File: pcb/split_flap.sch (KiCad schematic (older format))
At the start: 53 parts, among them T1 MPSA14, T2 2N6073B, T3 MPSU45, T4 PN2222A

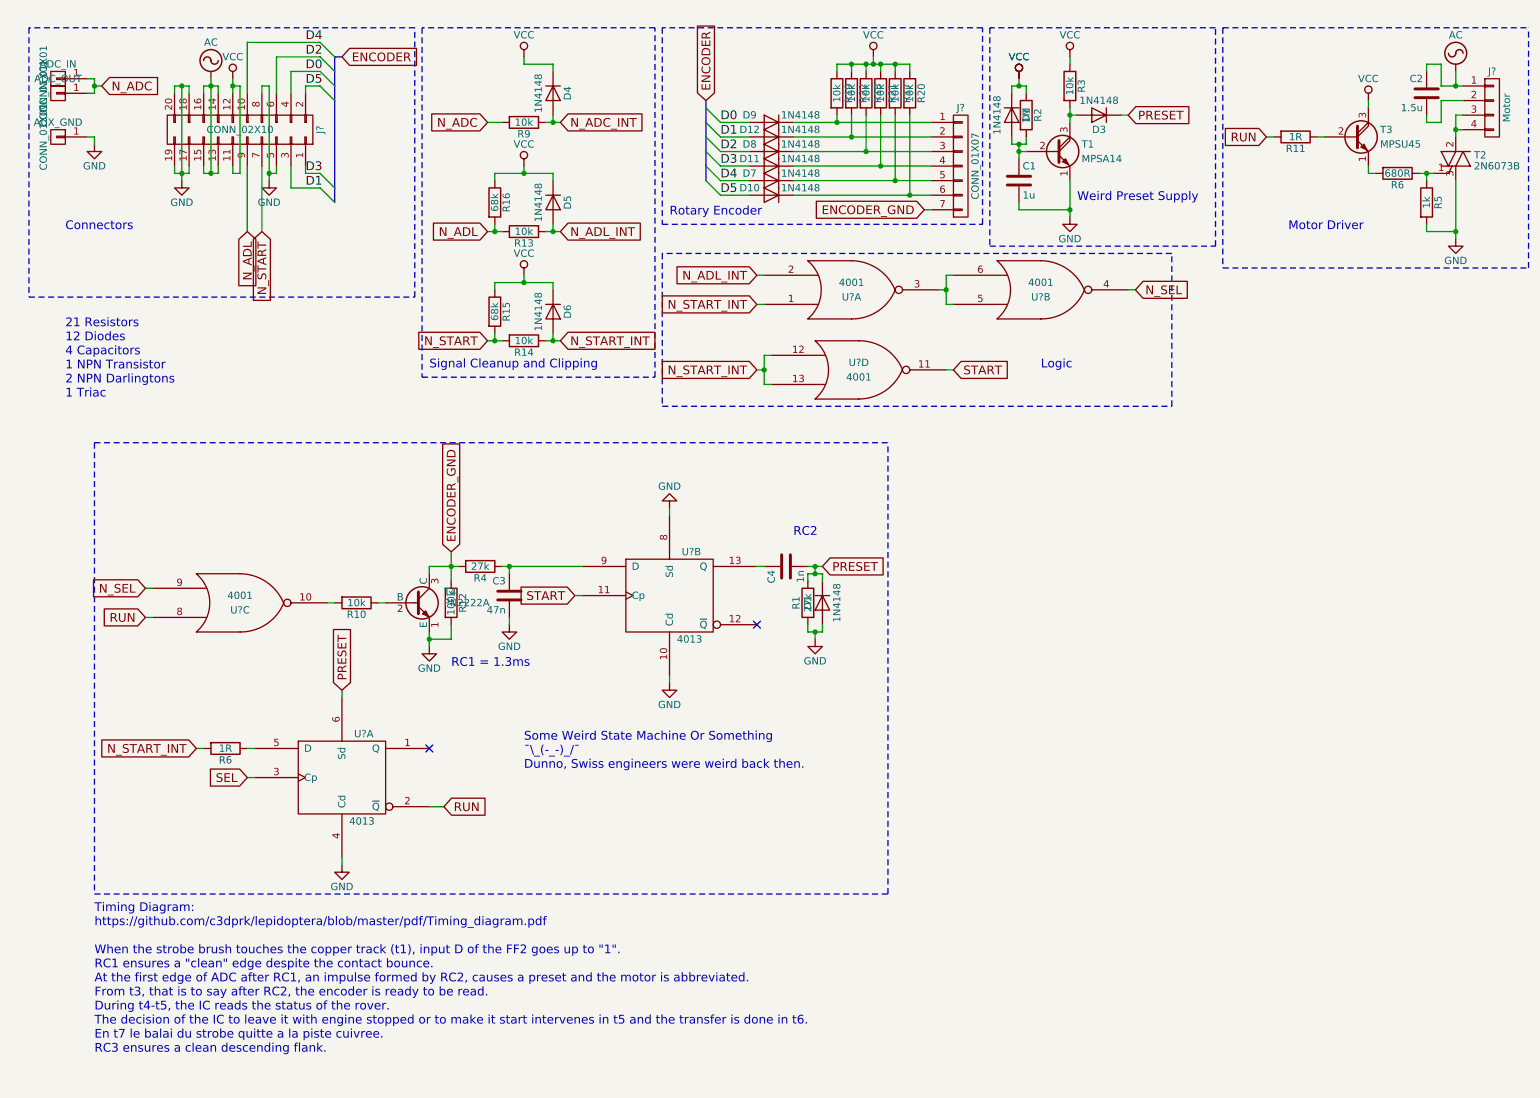
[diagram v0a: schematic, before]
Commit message: rearranged parts and refernce labels '
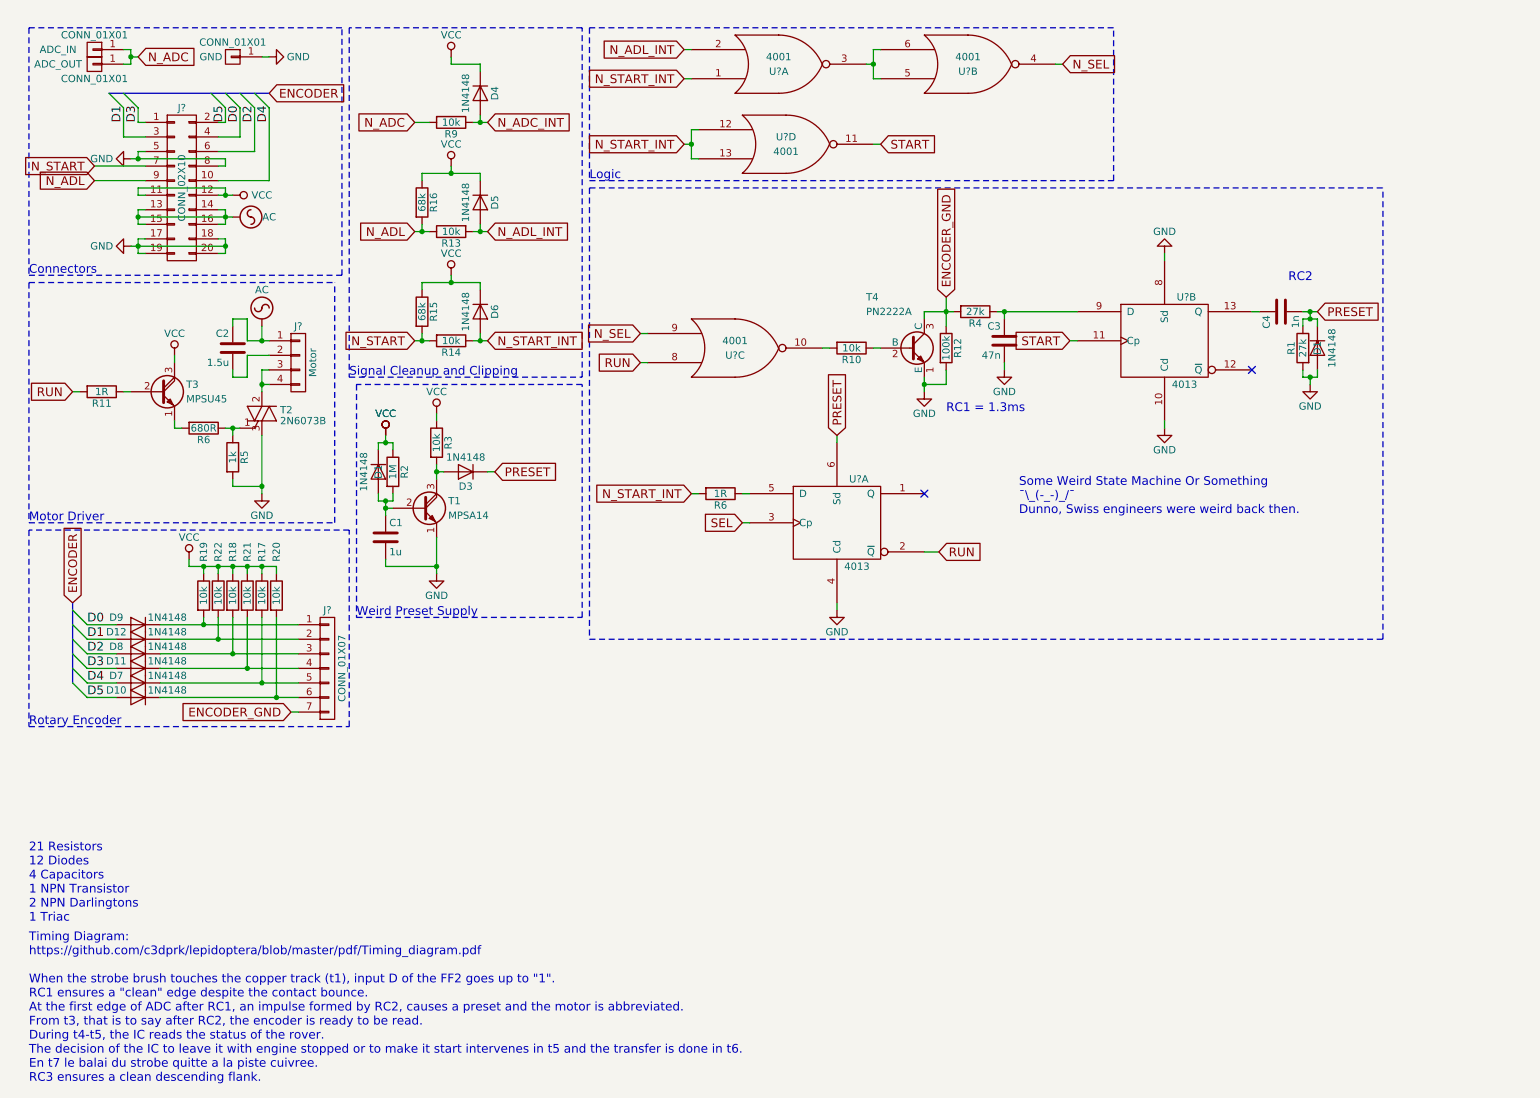
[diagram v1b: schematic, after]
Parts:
- renumbered AUX_GND to GND
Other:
- moved on the sheet: ADC_IN, ADC_OUT, C1, C2, C3, C4, D1, D10, D11, D12, D3, D4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
